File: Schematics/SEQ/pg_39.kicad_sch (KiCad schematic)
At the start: 22 parts, among them U4001 F280, U4002 F280, U4003 F280, U4004 F280, U4005 F280, U4006 F280, U4007 F280, U4008 F280, U4009 F240, U4010 F521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

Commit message: Much work on SEQ
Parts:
- removed U4003, U4004, U4005, U4006, U4007, U4008: F280, symbol r1000:F280
- removed U4009: F240, symbol r1000:F240
- U4001: value F280 -> XPAR64; symbol r1000:F280 -> r1000:XPAR64; Location D44 -> x99; Name TPCHK0 -> TPCHK
- U4002: value F280 -> F244; symbol r1000:F280 -> r1000:F244; Location D41 -> A28; Name TPCHK1 -> TPDRVR
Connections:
- net TYPE_PEV0 is gone; now on net TYPE~3: U4001.5 (I3)
- net TYPE_PEV1 is gone; now on net Q.TYPE.P6: U4002.5 (Y6)
- net PD: now also U4001.1 (ODD); no longer U4001.13 (I5), U4002.13 (I5)
- net Q.TYPE.P0: now also U4002.18 (Y0)
- net Q.TYPE.P1: now also U4002.16 (Y1)
- net Q.TYPE.P2: now also U4002.14 (Y2)
- net Q.TYPE.P3: now also U4002.12 (Y3)
- net Q.TYPE.P4: now also U4002.9 (Y4)
- net Q.TYPE.P5: now also U4002.7 (Y5)
- net Q.TYPE.P7: now also U4002.3 (Y7)
- net TYPE_DRV~: now also U4002.1 (OE0), U4002.19 (OE1)
- net TYPE_POD0: now also U4001.66 (P0), U4002.2 (I0); no longer U4001.6 (POD)
- net TYPE_POD1: now also U4001.67 (P1), U4002.4 (I1); no longer U4002.6 (POD)
- net TYPE_POD2: now also U4001.68 (P2), U4002.6 (I2)
- net TYPE_POD3: now also U4001.69 (P3), U4002.8 (I3)
- net TYPE_POD4: now also U4001.70 (P4), U4002.11 (I4)
- net TYPE_POD5: now also U4001.71 (P5), U4002.13 (I5)
- net TYPE_POD6: now also U4001.72 (P6), U4002.15 (I6)
- net TYPE_POD7: now also U4001.73 (P7), U4002.17 (I7)
- net TYPE~0: now also U4001.2 (I0); no longer U4001.8 (I0)
- net TYPE~1: now also U4001.3 (I1); no longer U4001.2 (I7)
- net TYPE~10: now also U4001.12 (I10); no longer U4002.1 (I6)
- net TYPE~11: now also U4001.13 (I11); no longer U4002.4 (I8)
- net TYPE~12: now also U4001.14 (I12); no longer U4002.12 (I4)
- net TYPE~13: now also U4001.15 (I13); no longer U4002.10 (I2)
- net TYPE~14: now also U4001.16 (I14); no longer U4002.9 (I1)
- net TYPE~15: now also U4001.17 (I15); no longer U4002.11 (I3)
- net TYPE~16: now also U4001.18 (I16)
- net TYPE~17: now also U4001.19 (I17)
- net TYPE~18: now also U4001.20 (I18)
- net TYPE~19: now also U4001.21 (I19)
- net TYPE~2: now also U4001.4 (I2); no longer U4001.1 (I6)
- net TYPE~20: now also U4001.22 (I20)
- net TYPE~21: now also U4001.23 (I21)
- net TYPE~22: now also U4001.24 (I22)
- net TYPE~23: now also U4001.25 (I23)
- net TYPE~24: now also U4001.26 (I24)
- net TYPE~25: now also U4001.27 (I25)
- net TYPE~26: now also U4001.28 (I26)
- net TYPE~27: now also U4001.29 (I27)
- net TYPE~28: now also U4001.30 (I28)
- net TYPE~29: now also U4001.31 (I29)
- net TYPE~3: no longer U4001.4 (I8)
- net TYPE~30: now also U4001.32 (I30)
- net TYPE~31: now also U4001.33 (I31)
- net TYPE~32: now also U4001.34 (I32)
- net TYPE~33: now also U4001.35 (I33)
- net TYPE~34: now also U4001.36 (I34)
- net TYPE~35: now also U4001.37 (I35)
- net TYPE~36: now also U4001.38 (I36)
- net TYPE~37: now also U4001.39 (I37)
- net TYPE~38: now also U4001.40 (I38)
- net TYPE~39: now also U4001.41 (I39)
- net TYPE~4: now also U4001.6 (I4); no longer U4001.12 (I4)
- net TYPE~40: now also U4001.42 (I40)
- net TYPE~41: now also U4001.43 (I41)
- net TYPE~42: now also U4001.44 (I42)
- net TYPE~43: now also U4001.45 (I43)
- net TYPE~44: now also U4001.46 (I44)
- net TYPE~45: now also U4001.47 (I45)
- net TYPE~46: now also U4001.48 (I46)
- net TYPE~47: now also U4001.49 (I47)
- net TYPE~48: now also U4001.50 (I48)
- net TYPE~49: now also U4001.51 (I49)
- net TYPE~5: now also U4001.7 (I5); no longer U4001.10 (I2)
- net TYPE~50: now also U4001.52 (I50)
- net TYPE~51: now also U4001.53 (I51)
- net TYPE~52: now also U4001.54 (I52)
- net TYPE~53: now also U4001.55 (I53)
- net TYPE~54: now also U4001.56 (I54)
- net TYPE~55: now also U4001.57 (I55)
- net TYPE~56: now also U4001.58 (I56)
- net TYPE~57: now also U4001.59 (I57)
- net TYPE~58: now also U4001.60 (I58)
- net TYPE~59: now also U4001.61 (I59)
- net TYPE~6: now also U4001.8 (I6); no longer U4001.9 (I1)
- net TYPE~60: now also U4001.62 (I60)
- net TYPE~61: now also U4001.63 (I61)
- net TYPE~62: now also U4001.64 (I62)
- net TYPE~63: now also U4001.65 (I63)
- net TYPE~7: now also U4001.9 (I7); no longer U4001.11 (I3)
- net TYPE~8: now also U4001.10 (I8); no longer U4002.8 (I0)
- net TYPE~9: now also U4001.11 (I9); no longer U4002.2 (I7)
- no-connect marks 0 -> 1

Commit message: KiCad 6
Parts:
- GF140, GF142, GF144, GF146, GF160, GF162, GF164, GF166, GF293, GF296: value GF -> (none)
- U4001: value XPAR64 -> (none)
- U4002: value F244 -> (none)
- U4010: value F521 -> (none)
- U4011: value F51 -> (none)
- U4012: value F37 -> (none)

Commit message: Recover from KiCad-6 munging
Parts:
- GF140, GF142, GF144, GF146, GF160, GF162, GF164, GF166, GF293, GF296: value (none) -> GF
- U4001: value (none) -> XPAR64
- U4002: value (none) -> F244
- U4010: value (none) -> F521
- U4011: value (none) -> F51
- U4012: value (none) -> F37

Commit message: Snapshot
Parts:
- removed GF293: GF, symbol r1000:GF
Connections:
- net Q.BUZZ_OFF~ renamed Q1~
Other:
- note added: "Q.BUZZ_OFF~"
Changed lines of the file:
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@@
   (wire (pts (xy 279.4 294.64) (xy 287.02 294.64) ) )
   (wire (pts (xy 287.02 299.72) (xy 287.02 294.64) ) )
-  (wire (pts (xy 293.37 180.34) (xy 302.26 180.34) ) )
+  (wire (pts (xy 293.37 180.34) (xy 436.88 180.34) ) )
   (wire (pts (xy 294.64 144.78) (xy 302.26 144.78) ) )
   (wire (pts (xy 299.72 134.62) (xy 302.26 134.62) ) )
-  (wire (pts (xy 299.72 190.5) (xy 302.26 190.5) ) )
   (wire (pts (xy 299.72 314.96) (xy 342.9 314.96) ) )
   (wire (pts (xy 299.72 320.04) (xy 342.9 320.04) ) )
@@
   (wire (pts (xy 302.26 134.62) (xy 302.26 144.78) ) )
   (wire (pts (xy 302.26 144.78) (xy 355.6 144.78) ) )
-  (wire (pts (xy 302.26 180.34) (xy 436.88 180.34) ) )
-  (wire (pts (xy 302.26 190.5) (xy 302.26 180.34) ) )
   (wire (pts (xy 334.01 152.4) (xy 355.6 152.4) ) )
   (wire (pts (xy 334.01 172.72) (xy 360.68 172.72) ) )
@@
   (junction (at 279.4 294.64) (diameter 0) (color 0 0 0 0) )
   (symbol (lib_id "r1000:F244") (at 281.94 347.98 0) (unit 1) (in_bom yes) (on_board yes) (property "Reference" "U4002" (id 0) (at 284.48 342.9 0) (effects (font (size 1.27 1.27) ) ) ) (property "Value" "F244" (id 1) (at 278.13 355.6 0) (effects (font (size 2.54 2.54) ) (justify left) ) ) (property "Footprint" "" (id 2) (at 283.21 349.25 0) (effects (font (size 1.27 1.27) ) hide ) ) (property "Datasheet" "" (id 3) (at 283.21 349.25 0) (effects (font (size 1.27 1.27) ) hide ) ) (property "Location" "A28" (id 4) (at 280.67 347.98 0) (effects (font (size 2.54 2.54) ) (justify left) ) ) (property "Name" "TPDRVR" (id 5) (at 283.21 363.22 0) (effects (font (size 2.54 2.54) ) (justify bottom) ) ) (pin "1") (pin "11") (pin "12") (pin "13") (pin "14") (pin "15") (pin "16") (pin "17") (pin "18") (pin "19") (pin "2") (pin "3") (pin "4") (pin "5") (pin "6") (pin "7") (pin "8") (pin "9") )
-  (global_label "Q.BUZZ_OFF~" (shape input) (at 293.37 180.34 180) (fields_autoplaced) (effects (font (size 2.54 2.54) ) (justify right) ) (property "Intersheet References" "${INTERSHEET_REFS}" (id 0) (at 263.8697 180.1813 0) (effects (font (size 1.905 1.905) ) (justify right) ) ) )
+  (global_label "Q1~" (shape input) (at 293.37 180.34 180) (fields_autoplaced) (effects (font (size 2.54 2.54) ) (justify right) ) (property "Intersheet References" "${INTERSHEET_REFS}" (id 0) (at 280.7923 180.34 0) (effects (font (size 1.905 1.905) ) (justify right) ) ) )
   (global_label "Q.SEQ_TV.EN~" (shape input) (at 294.64 144.78 180) (fields_autoplaced) (effects (font (size 2.54 2.54) ) (justify right) ) (property "Intersheet References" "${INTERSHEET_REFS}" (id 0) (at 264.535 144.6213 0) (effects (font (size 1.905 1.905) ) (justify right) ) ) )
   (symbol (lib_id "r1000:GF") (at 299.72 134.62 0) (mirror y) (unit 1) (in_bom yes) (on_board yes) (property "Reference" "GF296" (id 0) (at 295.91 134.62 0) (effects (font (size 2.54 2.54) ) (justify left) ) ) (property "Value" "GF" (id 1) (at 299.72 134.62 0) (effects (font (size 1.27 1.27) ) hide ) ) (property "Footprint" "" (id 2) (at 299.72 134.62 0) (effects (font (size 1.27 1.27) ) hide ) ) (property "Datasheet" "" (id 3) (at 299.72 134.62 0) (effects (font (size 1.27 1.27) ) hide ) ) (pin "1") )
-  (symbol (lib_id "r1000:GF") (at 299.72 190.5 0) (mirror y) (unit 1) (in_bom yes) (on_board yes) (property "Reference" "GF293" (id 0) (at 295.91 190.5 0) (effects (font (size 2.54 2.54) ) (justify left) ) ) (property "Value" "GF" (id 1) (at 299.72 190.5 0) (effects (font (size 1.27 1.27) ) hide ) ) (property "Footprint" "" (id 2) (at 299.72 190.5 0) (effects (font (size 1.27 1.27) ) hide ) ) (property "Datasheet" "" (id 3) (at 299.72 190.5 0) (effects (font (size 1.27 1.27) ) hide ) ) (pin "1") )
   (junction (at 302.26 144.78) (diameter 0) (color 0 0 0 0) )
-  (junction (at 302.26 180.34) (diameter 0) (color 0 0 0 0) )
   (label "Q.TYPE.P0" (at 304.8 314.96 0) (effects (font (size 2.54 2.54) ) (justify left bottom) ) )
   (label "Q.TYPE.P1" (at 304.8 320.04 0) (effects (font (size 2.54 2.54) ) (justify left bottom) ) )
@@
   (symbol (lib_id "r1000:F51") (at 383.54 157.48 0) (unit 1) (in_bom yes) (on_board yes) (property "Reference" "U4011" (id 0) (at 396.24 156.21 0) (effects (font (size 1.27 1.27) ) ) ) (property "Value" "F51" (id 1) (at 385.445 162.56 0) (effects (font (size 2.54 2.54) ) ) ) (property "Footprint" "" (id 2) (at 383.54 162.56 0) (effects (font (size 1.27 1.27) ) hide ) ) (property "Datasheet" "" (id 3) (at 383.54 162.56 0) (effects (font (size 1.27 1.27) ) hide ) ) (property "Location" "A47" (id 4) (at 385.445 157.48 0) (effects (font (size 2.54 2.54) ) ) ) (property "Name" "BCAOI0A" (id 5) (at 388.62 170.18 0) (effects (font (size 2.54 2.54) ) (justify bottom) ) ) (pin "1") (pin "2") (pin "3") (pin "4") (pin "5") (pin "6") (pin "7") )
   (symbol (lib_id "r1000:PD") (at 388.62 299.72 0) (unit 1) (in_bom no) (on_board yes) (property "Reference" "#PWR04002" (id 0) (at 388.62 299.72 0) (effects (font (size 1.27 1.27) ) hide ) ) (property "Value" "PD" (id 1) (at 388.62 299.72 0) (effects (font (size 1.27 1.27) ) hide ) ) (property "Footprint" "" (id 2) (at 388.62 299.72 0) (effects (font (size 1.27 1.27) ) hide ) ) (property "Datasheet" "" (id 3) (at 388.62 299.72 0) (effects (font (size 1.27 1.27) ) hide ) ) (pin "1") )
+  (text "Q.BUZZ_OFF~" (at 398.78 180.34 0) (effects (font (size 2.54 2.54) ) (justify left bottom) ) )
   (symbol (lib_id "r1000:F521") (at 406.4 350.52 0) (unit 1) (in_bom yes) (on_board yes) (property "Reference" "U4010" (id 0) (at 408.94 345.44 0) (effects (font (size 1.27 1.27) ) ) ) (property "Value" "F521" (id 1) (at 402.59 358.14 0) (effects (font (size 2.54 2.54) ) (justify left) ) ) (property "Footprint" "" (id 2) (at 407.67 351.79 0) (effects (font (size 1.27 1.27) ) hide ) ) (property "Datasheet" "" (id 3) (at 407.67 351.79 0) (effects (font (size 1.27 1.27) ) hide ) ) (property "Location" "A29" (id 4) (at 405.13 350.52 0) (effects (font (size 2.54 2.54) ) (justify left) ) ) (property "Name" "TPCOMP" (id 5) (at 407.67 365.76 0) (effects (font (size 2.54 2.54) ) (justify bottom) ) ) (pin "1") (pin "11") (pin "12") (pin "13") (pin "14") (pin "15") (pin "16") (pin "17") (pin "18") (pin "19") (pin "2") (pin "3") (pin "4") (pin "5") (pin "6") (pin "7") (pin "8") (pin "9") )
   (global_label "TYP_PERR.MCHK" (shape output) (at 414.02 297.18 0) (fields_autoplaced) (effects (font (size 2.54 2.54) ) (justify left) ) (property "Intersheet References" "${INTERSHEET_REFS}" (id 0) (at 449.205 297.0213 0) (effects (font (size 1.905 1.905) ) (justify left) ) ) )

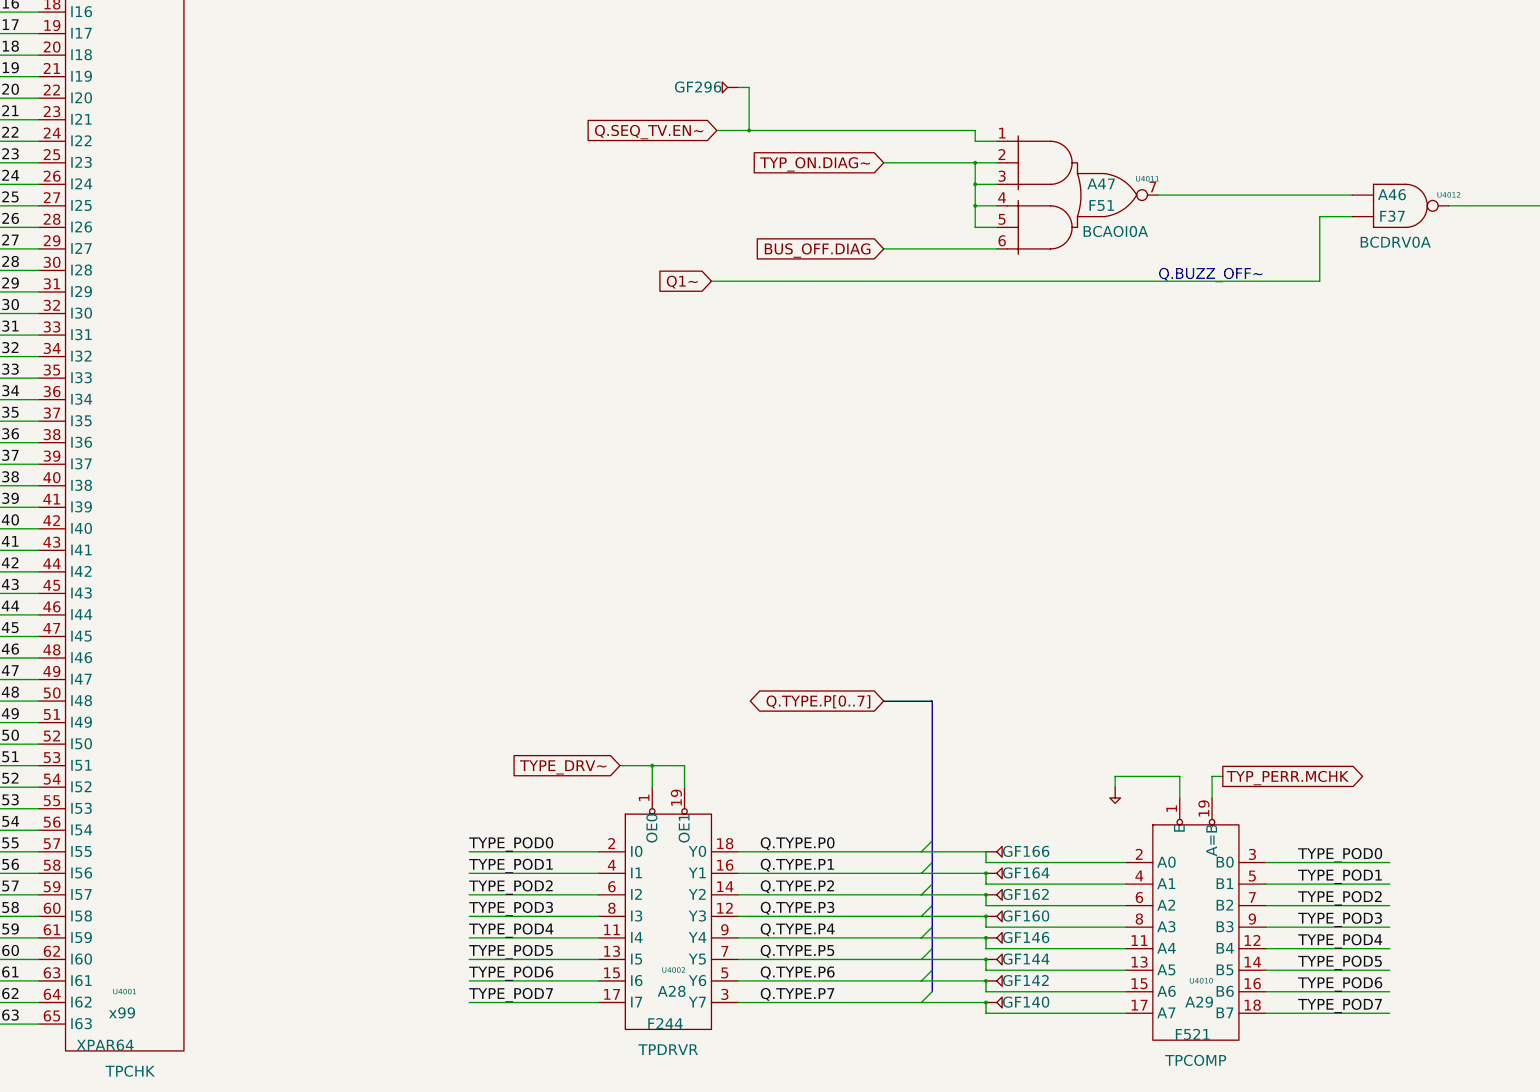
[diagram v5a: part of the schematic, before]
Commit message: Fix polarity of unused part of driven FIU bus.
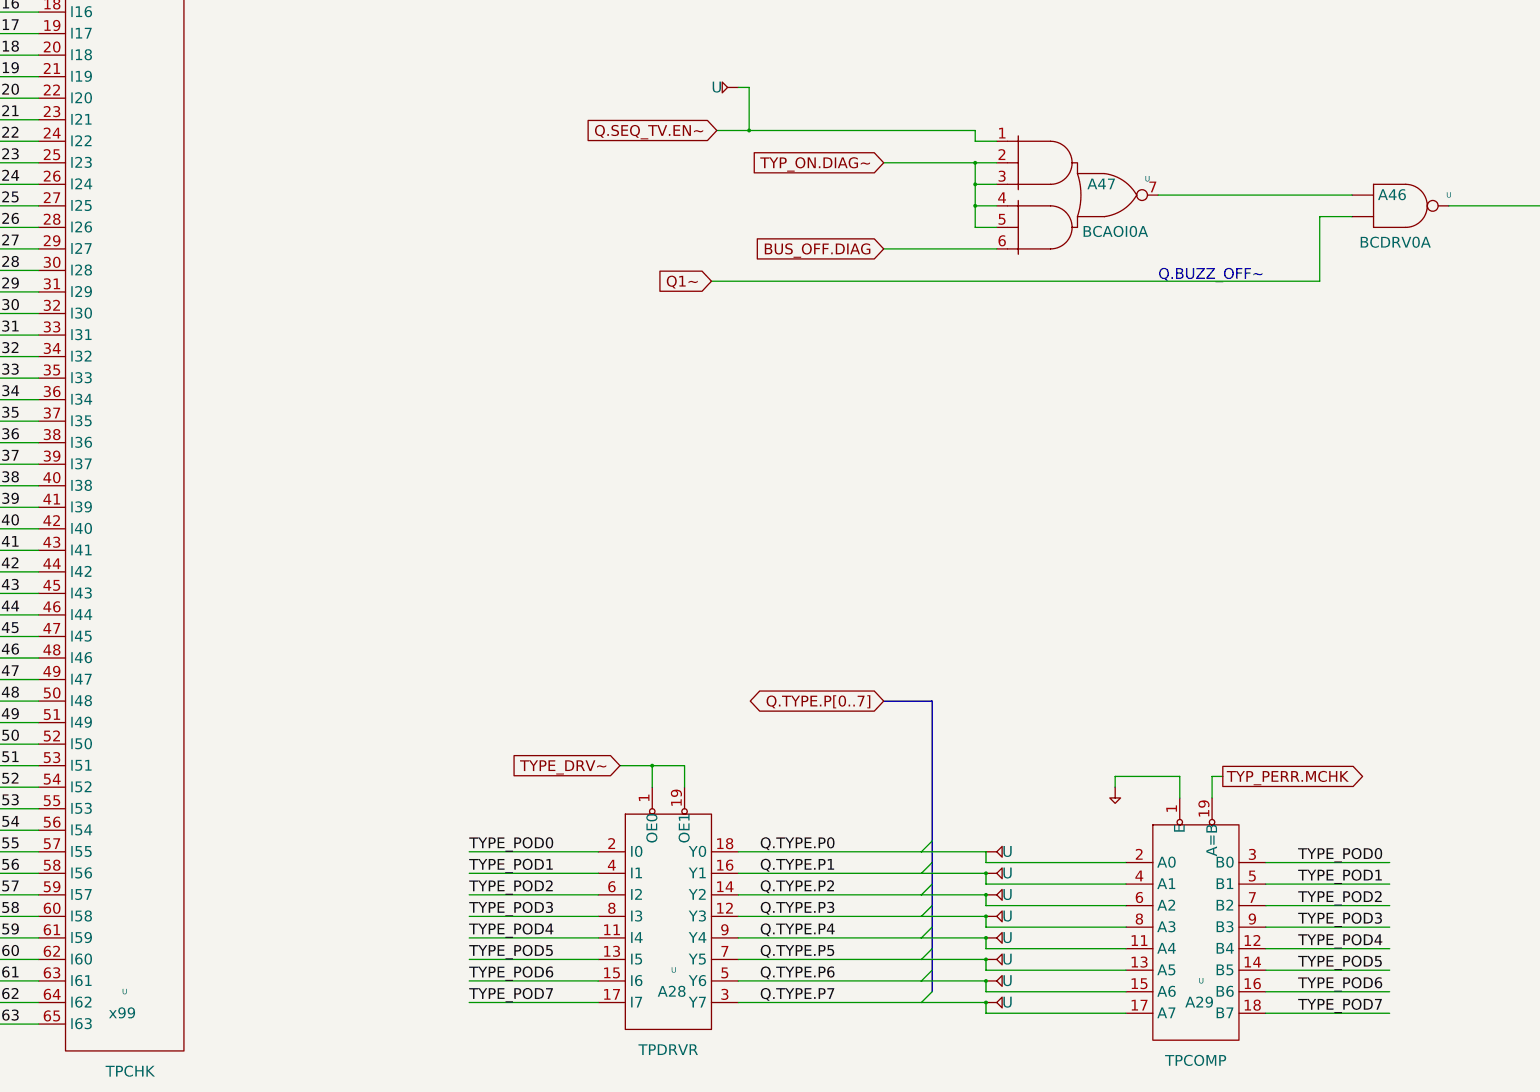
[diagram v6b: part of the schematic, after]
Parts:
- removed GF140, GF142, GF144, GF146, GF160, GF162, GF164, GF166, GF296: GF, symbol r1000:GF
- removed U4001: XPAR64, symbol r1000:XPAR64
- removed U4002: F244, symbol r1000:F244
- removed U4010: F521, symbol r1000:F521
- removed U4011: F51, symbol r1000:F51
- removed U4012: F37, symbol r1000:F37
- added U (x9): (no value), symbol r1000:GF
- added U: (no value), symbol r1000:F37
- added U: (no value), symbol r1000:F521
- added U: (no value), symbol r1000:F244
- added U: (no value), symbol r1000:XPAR64
- added U: (no value), symbol r1000:F51
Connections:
- net BUS_OFF.DIAG: now also U.6 (B3)
- net PD: now also U.1 (E), U.1 (ODD)
- net Q.SEQ_TV.EN~: now also U.1, U.1 (A1)
- net Q.TYPE.P0: now also U.1, U.18 (Y0), U.2 (A0)
- net Q.TYPE.P1: now also U.1, U.16 (Y1), U.4 (A1)
- net Q.TYPE.P2: now also U.1, U.14 (Y2), U.6 (A2)
- net Q.TYPE.P3: now also U.1, U.12 (Y3), U.8 (A3)
- net Q.TYPE.P4: now also U.1, U.11 (A4), U.9 (Y4)
- net Q.TYPE.P5: now also U.1, U.13 (A5), U.7 (Y5)
- net Q.TYPE.P6: now also U.1, U.15 (A6), U.5 (Y6)
- net Q.TYPE.P7: now also U.1, U.17 (A7), U.3 (Y7)
- net Q1~: now also U.2 (D1)
- net TYPE_DRV~: now also U.1 (OE0), U.19 (OE1), U.3 (Q)
- net TYPE_POD0: now also U.2 (I0), U.3 (B0), U.66 (P0)
- net TYPE_POD1: now also U.4 (I1), U.5 (B1), U.67 (P1)
- net TYPE_POD2: now also U.6 (I2), U.68 (P2), U.7 (B2)
- net TYPE_POD3: now also U.69 (P3), U.8 (I3), U.9 (B3)
- net TYPE_POD4: now also U.11 (I4), U.12 (B4), U.70 (P4)
- net TYPE_POD5: now also U.13 (I5), U.14 (B5), U.71 (P5)
- net TYPE_POD6: now also U.15 (I6), U.16 (B6), U.72 (P6)
- net TYPE_POD7: now also U.17 (I7), U.18 (B7), U.73 (P7)
- net TYPE~0: now also U.2 (I0)
- net TYPE~1: now also U.3 (I1)
- net TYPE~10: now also U.12 (I10)
- net TYPE~11: now also U.13 (I11)
- net TYPE~12: now also U.14 (I12)
- net TYPE~13: now also U.15 (I13)
- net TYPE~14: now also U.16 (I14)
- net TYPE~15: now also U.17 (I15)
- net TYPE~16: now also U.18 (I16)
- net TYPE~17: now also U.19 (I17)
- net TYPE~18: now also U.20 (I18)
- net TYPE~19: now also U.21 (I19)
- net TYPE~2: now also U.4 (I2)
- net TYPE~20: now also U.22 (I20)
- net TYPE~21: now also U.23 (I21)
- net TYPE~22: now also U.24 (I22)
- net TYPE~23: now also U.25 (I23)
- net TYPE~24: now also U.26 (I24)
- net TYPE~25: now also U.27 (I25)
- net TYPE~26: now also U.28 (I26)
- net TYPE~27: now also U.29 (I27)
- net TYPE~28: now also U.30 (I28)
- net TYPE~29: now also U.31 (I29)
- net TYPE~3: now also U.5 (I3)
- net TYPE~30: now also U.32 (I30)
- net TYPE~31: now also U.33 (I31)
- net TYPE~32: now also U.34 (I32)
- net TYPE~33: now also U.35 (I33)
- net TYPE~34: now also U.36 (I34)
- net TYPE~35: now also U.37 (I35)
- net TYPE~36: now also U.38 (I36)
- net TYPE~37: now also U.39 (I37)
- net TYPE~38: now also U.40 (I38)
- net TYPE~39: now also U.41 (I39)
- net TYPE~4: now also U.6 (I4)
- net TYPE~40: now also U.42 (I40)
- net TYPE~41: now also U.43 (I41)
- net TYPE~42: now also U.44 (I42)
- net TYPE~43: now also U.45 (I43)
- net TYPE~44: now also U.46 (I44)
- net TYPE~45: now also U.47 (I45)
- net TYPE~46: now also U.48 (I46)
- net TYPE~47: now also U.49 (I47)
- net TYPE~48: now also U.50 (I48)
- net TYPE~49: now also U.51 (I49)
- net TYPE~5: now also U.7 (I5)
- net TYPE~50: now also U.52 (I50)
- net TYPE~51: now also U.53 (I51)
- net TYPE~52: now also U.54 (I52)
- net TYPE~53: now also U.55 (I53)
- net TYPE~54: now also U.56 (I54)
- net TYPE~55: now also U.57 (I55)
- net TYPE~56: now also U.58 (I56)
- net TYPE~57: now also U.59 (I57)
- net TYPE~58: now also U.60 (I58)
- net TYPE~59: now also U.61 (I59)
- net TYPE~6: now also U.8 (I6)
- net TYPE~60: now also U.62 (I60)
- net TYPE~61: now also U.63 (I61)
- net TYPE~62: now also U.64 (I62)
- net TYPE~63: now also U.65 (I63)
- net TYPE~7: now also U.9 (I7)
- net TYPE~8: now also U.10 (I8)
- net TYPE~9: now also U.11 (I9)
- net TYP_ON.DIAG~: now also U.2 (A2), U.3 (A3), U.4 (B1), U.5 (B2)
- net TYP_PERR.MCHK: now also U.19 (A=B)
- new net: U.1 (D0), U.7 (Q)
